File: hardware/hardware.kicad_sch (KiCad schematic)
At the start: 72 parts, among them J1 VBAT+, J10 Conn_01x05_Pin, J2 GND, J3 PHASE_A, J4 PHASE_B, J5 PHASE_C, J6 VBAT+, J7 GND, Q1 SiR158DP, Q10 SiR158DP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

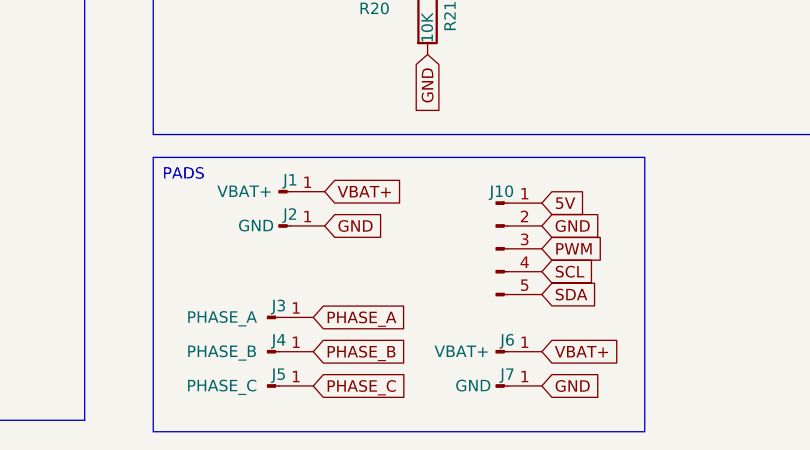
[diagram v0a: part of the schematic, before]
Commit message: add rev1 board - single side
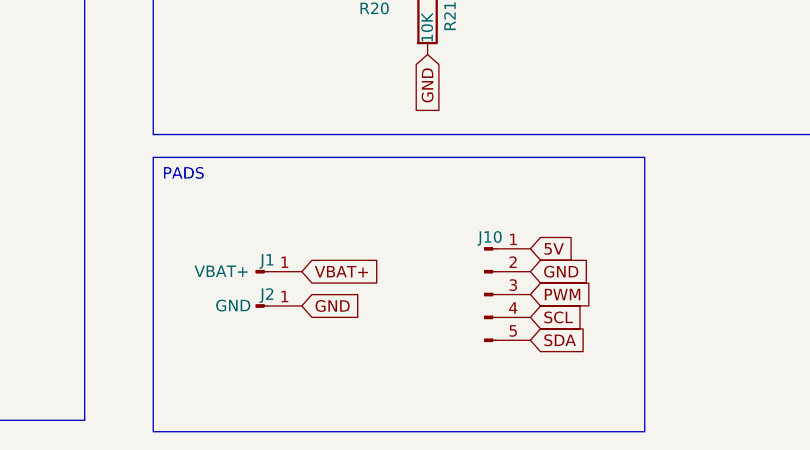
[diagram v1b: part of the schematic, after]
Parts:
- removed J3: PHASE_A, TestPoint:TestPoint_Pad_1.0x1.0mm, symbol Connector:Conn_01x01_Pin
- removed J4: PHASE_B, TestPoint:TestPoint_Pad_1.0x1.0mm, symbol Connector:Conn_01x01_Pin
- removed J5: PHASE_C, TestPoint:TestPoint_Pad_1.0x1.0mm, symbol Connector:Conn_01x01_Pin
- removed J6: VBAT+, TestPoint:TestPoint_Pad_2.0x2.0mm, symbol Connector:Conn_01x01_Pin
- removed J7: GND, TestPoint:TestPoint_Pad_2.0x2.0mm, symbol Connector:Conn_01x01_Pin
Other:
- moved on the sheet: J1, J10, J2

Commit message: add rev2
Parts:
- removed C4: 0.1uF, Capacitor_SMD:C_0805_2012Metric_Pad1.18x1.45mm_HandSolder, symbol Device:C
- removed C5: 1uF, Capacitor_SMD:C_0805_2012Metric_Pad1.18x1.45mm_HandSolder, symbol Device:C
- removed C6, C7, C8, C9: 100uF, Capacitor_Tantalum_SMD:CP_EIA-3216-10_Kemet-I, symbol Device:C_Polarized
- removed D1: BLUE, LED_SMD:LED_0805_2012Metric_Pad1.15x1.40mm_HandSolder, symbol Device:LED
- removed D2: RED, LED_SMD:LED_0805_2012Metric_Pad1.15x1.40mm_HandSolder, symbol Device:LED
- removed J10: Conn_01x05_Pin, Connector_JST:JST_SH_BM05B-SRSS-TB_1x05-1MP_P1.00mm_Vertical, symbol Connector:Conn_01x05_Pin
- removed R10, R8: 3.3K, Resistor_SMD:R_0805_2012Metric_Pad1.20x1.40mm_HandSolder, symbol Device:R
- removed R2, R3: 10K, Resistor_SMD:R_0805_2012Metric_Pad1.20x1.40mm_HandSolder, symbol Device:R
- removed R5: 1K, Resistor_SMD:R_0805_2012Metric_Pad1.20x1.40mm_HandSolder, symbol Device:R
- removed R6: 4.7K, Resistor_SMD:R_0805_2012Metric_Pad1.20x1.40mm_HandSolder, symbol Device:R
- removed R7: 47K, Resistor_SMD:R_0805_2012Metric_Pad1.20x1.40mm_HandSolder, symbol Device:R
- removed R9: 18K, Resistor_SMD:R_0805_2012Metric_Pad1.20x1.40mm_HandSolder, symbol Device:R
- removed TH1: 10K, Resistor_SMD:R_0805_2012Metric_Pad1.20x1.40mm_HandSolder, symbol Device:Thermistor_NTC
- removed U2: ACS7122, Package_SO:SOIC-8_3.9x4.9mm_P1.27mm, symbol Sensor_Current:ACS712xLCTR-30A
- added J3: GND, TestPoint:TestPoint_Keystone_5015_Micro-Minature, symbol Connector:Conn_01x01_Pin
- added J4: PWM, TestPoint:TestPoint_Keystone_5015_Micro-Minature, symbol Connector:Conn_01x01_Pin
- J1: value VBAT+ -> VBAT
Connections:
- net VBAT+ is gone; now on net VBAT: J1.1 (Pin_1), U3.1 (IN)
- net GND: now also J3.1 (Pin_1)
- net PWM: now also J4.1 (Pin_1)
- net CURRENT_ADC: no longer names the net of U1.26 (PC3)
- net LED_STATUS: no longer names the net of U1.14 (PB2)
- net LED_WARN: no longer names the net of U1.13 (PB1)
- net SCL: no longer names the net of U1.28 (PC5)
- net SDA: no longer names the net of U1.27 (PC4)
- net TEMP_ADC: no longer names the net of U1.22 (ADC7)
- net VBAT_ADC: no longer names the net of U1.19 (ADC6)
- no-connect marks 7 -> 13
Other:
- moved on the sheet: C10, C2, C3, J1, J2, R11, R12, R13, R14, R15, R16, R17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

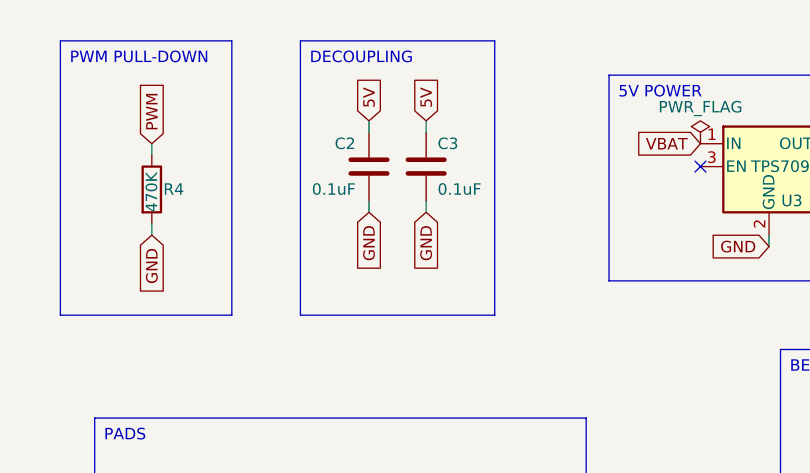
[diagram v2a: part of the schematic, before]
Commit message: rename capacitors
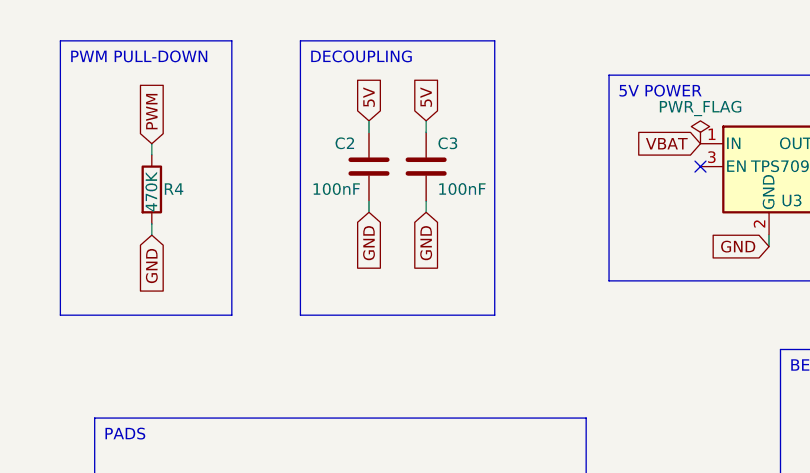
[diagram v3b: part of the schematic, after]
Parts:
- C2, C3: value 0.1uF -> 100nF
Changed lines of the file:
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@@
 			)
 		)
-		(property "Value" "0.1uF"
+		(property "Value" "100nF"
 			(at 156.21 33.02 0)
 			(effects
@@
 			)
 		)
-		(property "Value" "0.1uF"
+		(property "Value" "100nF"
 			(at 170.18 33.02 0)
 			(effects

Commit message: update rev3 board
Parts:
- J3, J4: footprint TestPoint:TestPoint_Keystone_5015_Micro-Minature -> TestPoint:TestPoint_Keystone_5015_Micro_Mini
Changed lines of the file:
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@@
 (kicad_sch
-	(version 20231120)
+	(version 20250114)
 	(generator "eeschema")
-	(generator_version "8.0")
+	(generator_version "9.0")
 	(paper "A4")
 	(title_block
 		(title "NoahESC")
-		(rev "2")
+		(rev "3")
+	)
+	(text_box "MCU"
+		(exclude_from_sim no)
+		(at 15.24 13.97 0)
+		(size 104.14 82.55)
+		(margins 0.9525 0.9525 0.9525 0.9525)
+		(stroke
+			(width 0)
+			(type default)
+		)
+		(fill
+			(type none)
+		)
+		(effects
+			(font
+				(size 1.27 1.27)
+			)
+			(justify left top)
+		)
+	)
+	(text_box "BEMF"
+		(exclude_from_sim no)
+		(at 208.28 50.8 0)
+		(size 58.42 45.72)
+		(margins 0.9525 0.9525 0.9525 0.9525)
+		(stroke
+			(width 0)
+			(type default)
+		)
+		(fill
+			(type none)
+		)
+		(effects
+			(font
+				(size 1.27 1.27)
+			)
+			(justify left top)
+		)
+	)
+	(text_box "5V POWER\n"
+		(exclude_from_sim no)
+		(at 189.23 20.32 0)
+		(size 34.29 22.86)
+		(margins 0.9525 0.9525 0.9525 0.9525)
+		(stroke
+			(width 0)
+			(type default)
+		)
+		(fill
+			(type none)
+		)
+		(effects
+			(font
+				(size 1.27 1.27)
+			)
+			(justify left top)
+		)
+	)
+	(text_box "PADS"
+		(exclude_from_sim no)
+		(at 132.08 58.42 0)
+		(size 54.61 30.48)
+		(margins 0.9525 0.9525 0.9525 0.9525)
+		(stroke
+			(width 0)
+			(type default)
+		)
+		(fill
+			(type none)
+		)
+		(effects
+			(font
+				(size 1.27 1.27)
+			)
+			(justify left top)
+		)
+	)
+	(text_box "DECOUPLING"
+		(exclude_from_sim no)
+		(at 154.94 16.51 0)
+		(size 21.59 30.48)
+		(margins 0.9525 0.9525 0.9525 0.9525)
+		(stroke
+			(width 0)
+			(type default)
+		)
+		(fill
+			(type none)
+		)
+		(effects
+			(font
+				(size 1.27 1.27)
+			)
+			(justify left top)
+		)
+	)
+	(text_box "MOSFET DRIVERS"
+		(exclude_from_sim no)
+		(at 105.41 104.14 0)
+		(size 170.18 55.88)
+		(margins 0.9525 0.9525 0.9525 0.9525)
+		(stroke
+			(width 0)
+			(type default)
+		)
+		(fill
+			(type none)
+		)
+		(effects
+			(font
+				(size 1.27 1.27)
+			)
+			(justify left top)
+		)
+	)
+	(text_box "PWM PULL-DOWN"
+		(exclude_from_sim no)
+		(at 128.27 16.51 0)
+		(size 19.05 30.48)
+		(margins 0.9525 0.9525 0.9525 0.9525)
+		(stroke
+			(width 0)
+			(type default)
+		)
+		(fill
+			(type none)
+		)
+		(effects
+			(font
+				(size 1.27 1.27)
+			)
+			(justify left top)
+		)
+	)
+	(text_box "MOSFETS"
+		(exclude_from_sim no)
+		(at 16.51 100.33 0)
+		(size 81.28 91.44)
+		(margins 0.9525 0.9525 0.9525 0.9525)
+		(stroke
+			(width 0)
+			(type default)
+		)
+		(fill
+			(type none)
+		)
+		(effects
+			(font
+				(size 1.27 1.27)
+			)
+			(justify left top)
+		)
 	)
 	(junction
@@
 		)
 	)
-	(text_box "MCU"
-		(exclude_from_sim no)
-		(at 15.24 13.97 0)
-		(size 104.14 82.55)
-		(stroke
-			(width 0)
-			(type default)
-		)
-		(fill
-			(type none)
-		)
-		(effects
-			(font
-				(size 1.27 1.27)
-			)
-			(justify left top)
-		)
-	)
-	(text_box "BEMF"
-		(exclude_from_sim no)
-		(at 208.28 50.8 0)
-		(size 58.42 45.72)
-		(stroke
-			(width 0)
-			(type default)
-		)
-		(fill
-			(type none)
-		)
-		(effects
-			(font
-				(size 1.27 1.27)
-			)
-			(justify left top)
-		)
-	)
-	(text_box "5V POWER\n"
-		(exclude_from_sim no)
-		(at 189.23 20.32 0)
-		(size 34.29 22.86)
-		(stroke
-			(width 0)
-			(type default)
-		)
-		(fill
-			(type none)
-		)
-		(effects
-			(font
-				(size 1.27 1.27)
-			)
-			(justify left top)
-		)
-	)
-	(text_box "PADS"
-		(exclude_from_sim no)
-		(at 132.08 58.42 0)
-		(size 54.61 30.48)
-		(stroke
-			(width 0)
-			(type default)
-		)
-		(fill
-			(type none)
-		)
-		(effects
-			(font
-				(size 1.27 1.27)
-			)
-			(justify left top)
-		)
-	)
-	(text_box "DECOUPLING"
-		(exclude_from_sim no)
-		(at 154.94 16.51 0)
-		(size 21.59 30.48)
-		(stroke
-			(width 0)
-			(type default)
-		)
-		(fill
-			(type none)
-		)
-		(effects
-			(font
-				(size 1.27 1.27)
-			)
-			(justify left top)
-		)
-	)
-	(text_box "MOSFET DRIVERS"
-		(exclude_from_sim no)
-		(at 105.41 104.14 0)
-		(size 170.18 55.88)
-		(stroke
-			(width 0)
-			(type default)
-		)
-		(fill
-			(type none)
-		)
-		(effects
-			(font
-				(size 1.27 1.27)
-			)
-			(justify left top)
-		)
-	)
-	(text_box "PWM PULL-DOWN"
-		(exclude_from_sim no)
-		(at 128.27 16.51 0)
-		(size 19.05 30.48)
-		(stroke
-			(width 0)
-			(type default)
-		)
-		(fill
-			(type none)
-		)
-		(effects
-			(font
-				(size 1.27 1.27)
-			)
-			(justify left top)
-		)
-	)
-	(text_box "MOSFETS"
-		(exclude_from_sim no)
-		(at 16.51 100.33 0)
-		(size 81.28 91.44)
-		(stroke
-			(width 0)
-			(type default)
-		)
-		(fill
-			(type none)
-		)
-		(effects
-			(font
-				(size 1.27 1.27)
-			)
-			(justify left top)
-		)
-	)
 	(global_label "PWM_BH"
 		(shape input)
@@
 			)
 		)
-		(property "Description" ""
+		(property "Description" "Generic connector, single row, 01x01, script generated"
 			(at 142.24 73.66 0)
 			(effects
@@
 		(fields_autoplaced yes)
 		(property "Reference" "Q9"
-			(at 248.92 124.46 0)
+			(at 248.92 124.4599 0)
 			(effects
 				(font
@@
 		)
 		(property "Value" "BC817"
-			(at 248.92 127 0)
+			(at 248.92 126.9999 0)
 			(effects
 				(font
@@
 			)
 		)
-		(property "Description" ""
+		(property "Description" "0.8A Ic, 45V Vce, NPN Transistor, SOT-23"
 			(at 243.84 125.73 0)
 			(effects
@@
 		(fields_autoplaced yes)
 		(property "Reference" "Q8"
-			(at 193.04 124.46 0)
+			(at 193.04 124.4599 0)
 			(effects
 				(font
@@
 		)
 		(property "Value" "BC817"
-			(at 193.04 127 0)
+			(at 193.04 126.9999 0)
 			(effects
 				(font
@@
 			)
 		)
-		(property "Description" ""
+		(property "Description" "0.8A Ic, 45V Vce, NPN Transistor, SOT-23"
 			(at 187.96 125.73 0)
 			(effects
@@
 			)
 		)
-		(property "Description" ""
+		(property "Description" "Generic connector, single row, 01x01, script generated"
 			(at 142.24 69.85 0)
 			(effects
@@
 		(fields_autoplaced yes)
 		(property "Reference" "Q7"
-			(at 135.89 125.73 0)
+			(at 135.89 125.7299 0)
 			(effects
 				(font
@@
 		)
 		(property "Value" "BC817"
-			(at 135.89 128.27 0)
+			(at 135.89 128.2699 0)
 			(effects
 				(font
@@
 			)
 		)
-		(property "Description" ""
+		(property "Description" "0.8A Ic, 45V Vce, NPN Transistor, SOT-23"
 			(at 130.81 127 0)
 			(effects
@@
 			)
 		)
-		(property "Footprint" "TestPoint:TestPoint_Keystone_5015_Micro-Minature"
+		(property "Footprint" "TestPoint:TestPoint_Keystone_5015_Micro_Mini"
 			(at 163.83 73.66 0)
 			(effects
@@
 			)
 		)
-		(property "Description" ""
+		(property "Description" "Generic connector, single row, 01x01, script generated"
 			(at 163.83 73.66 0)
 			(effects
@@
 			)
 		)
-		(property "Footprint" "TestPoint:TestPoint_Keystone_5015_Micro-Minature"
+		(property "Footprint" "TestPoint:TestPoint_Keystone_5015_Micro_Mini"
 			(at 163.83 68.58 0)
 			(effects
@@
 			)
 		)
-		(property "Description" ""
+		(property "Description" "Generic connector, single row, 01x01, script generated"
 			(at 163.83 68.58 0)
 			(effects
@@
 		)
 	)
+	(embedded_fonts no)
 )

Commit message: add rev4
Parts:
- added J5: Programming, Connector_PinHeader_1.27mm:PinHeader_1x06_P1.27mm_Vertical, symbol Connector:Conn_01x06_Pin
- C10, C11, C12, C13: LCSC (none) -> C28323
- C2, C3: LCSC (none) -> C49678
- D3, D4, D5: LCSC (none) -> C241939
- Q1, Q10, Q2, Q3, Q4, Q5: LCSC (none) -> C142530
- Q7, Q8, Q9: LCSC (none) -> C39828
- R11, R12, R13, R14, R15, R16: LCSC (none) -> C17713
- R17, R18, R19, R22, R25, R30: LCSC (none) -> C17673
- R20, R23, R26, R29, R31, R34: LCSC (none) -> C17408
- R21, R27, R32: LCSC (none) -> C84376
- R24, R28, R33: LCSC (none) -> C17520
- R4: LCSC (none) -> C89104
- U1: LCSC (none) -> C16190
- U3: LCSC (none) -> C2865456
- Y1: LCSC (none) -> C882606
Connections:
- net 5V: now also J5.2 (Pin_2)
- net GND: now also J5.1 (Pin_1)
- net MISO: now reaches U1.16 (PB4)
- net MISO: now also J5.4 (Pin_4)
- net SCK: now reaches U1.17 (PB5)
- net SCK: now also J5.6 (Pin_6)
- net RESET: now reaches U1.29 (PC6/~{RESET})
- net RESET: now also J5.3 (Pin_3)
- net PWM_CL renamed MOSI
- net MOSI: now also J5.5 (Pin_5)
- no-connect marks 13 -> 10
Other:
- moved on the sheet: J1, J2, J3, J4

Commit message: add new pwm pin
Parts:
- removed J3: GND, TestPoint:TestPoint_Keystone_5015_Micro_Mini, symbol Connector:Conn_01x01_Pin
- removed J4: PWM, TestPoint:TestPoint_Keystone_5015_Micro_Mini, symbol Connector:Conn_01x01_Pin
- added J6: PWM, Connector_PinHeader_2.54mm:PinHeader_1x02_P2.54mm_Vertical, symbol Connector:Conn_01x02_Pin
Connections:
- net GND: now also J6.1 (Pin_1)
- net PWM: now also J6.2 (Pin_2)
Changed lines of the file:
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@@
 		)
 	)
-	(global_label "PWM"
-		(shape input)
-		(at 147.32 81.28 0)
-		(fields_autoplaced yes)
-		(effects
-			(font
-				(size 1.27 1.27)
-			)
-			(justify left)
-		)
-		(property "Intersheetrefs" "${INTERSHEET_REFS}"
-			(at 154.478 81.28 0)
-			(effects
-				(font
-					(size 1.27 1.27)
-				)
-				(justify left)
-				(hide yes)
-			)
-		)
-	)
 	(global_label "PWM_BL"
 		(shape input)
@@
 		)
 	)
+	(global_label "PWM"
+		(shape input)
+		(at 144.78 80.01 0)
+		(fields_autoplaced yes)
+		(effects
+			(font
+				(size 1.27 1.27)
+			)
+			(justify left)
+		)
+		(property "Intersheetrefs" "${INTERSHEET_REFS}"
+			(at 151.938 80.01 0)
+			(effects
+				(font
+					(size 1.27 1.27)
+				)
+				(justify left)
+				(hide yes)
+			)
+		)
+	)
 	(global_label "PWM_BL"
 		(shape input)
@@
 	(global_label "GND"
 		(shape input)
+		(at 144.78 77.47 0)
+		(fields_autoplaced yes)
+		(effects
+			(font
+				(size 1.27 1.27)
+			)
+			(justify left)
+		)
+		(property "Intersheetrefs" "${INTERSHEET_REFS}"
+			(at 151.6357 77.47 0)
+			(effects
+				(font
+					(size 1.27 1.27)
+				)
+				(justify left)
+				(hide yes)
+			)
+		)
+	)
+	(global_label "GND"
+		(shape input)
 		(at 39.37 132.08 270)
 		(fields_autoplaced yes)
@@
 		)
 	)
-	(global_label "GND"
-		(shape input)
-		(at 147.32 76.2 0)
-		(fields_autoplaced yes)
-		(effects
-			(font
-				(size 1.27 1.27)
-			)
-			(justify left)
-		)
-		(property "Intersheetrefs" "${INTERSHEET_REFS}"
-			(at 154.1757 76.2 0)
-			(effects
-				(font
-					(size 1.27 1.27)
-				)
-				(justify left)
-				(hide yes)
-			)
-		)
-	)
 	(global_label "GATE_AH"
 		(shape input)
@@
 	)
 	(symbol
+		(lib_id "Connector:Conn_01x02_Pin")
+		(at 139.7 77.47 0)
+		(unit 1)
+		(exclude_from_sim no)
+		(in_bom yes)
+		(on_board yes)
+		(dnp no)
+		(property "Reference" "J6"
+			(at 141.224 74.93 0)
+			(effects
+				(font
+					(size 1.27 1.27)
+				)
+			)
+		)
+		(property "Value" "PWM"
+			(at 136.144 78.74 0)
+			(effects
+				(font
+					(size 1.27 1.27)
+				)
+			)
+		)
+		(property "Footprint" "Connector_PinHeader_2.54mm:PinHeader_1x02_P2.54mm_Vertical"
+			(at 139.7 77.47 0)
+			(effects
+				(font
+					(size 1.27 1.27)
+				)
+				(hide yes)
+			)
+		)
+		(property "Datasheet" "~"
+			(at 139.7 77.47 0)
+			(effects
+				(font
+					(size 1.27 1.27)
+				)
+				(hide yes)
+			)
+		)
+		(property "Description" "Generic connector, single row, 01x02, script generated"
+			(at 139.7 77.47 0)
+			(effects
+				(font
+					(size 1.27 1.27)
+				)
+				(hide yes)
+			)
+		)
+		(property "LCSC" "C42431798"
+			(at 139.7 77.47 0)
+			(effects
+				(font
+					(size 1.27 1.27)
+				)
+				(hide yes)
+			)
+		)
+		(pin "1"
+		)
+		(pin "2"
+		)
+		(instances
+			(project ""
+				(path "/db766d7c-2ba8-4022-adcf-07c3b0e5779a"
+					(reference "J6")
+					(unit 1)
+				)
+			)
+		)
+	)
+	(symbol
 		(lib_id "Device:C")
 		(at 162.56 30.48 0)
@@
 	)
 	(symbol
-		(lib_id "Connector:Conn_01x01_Pin")
-		(at 142.24 81.28 0)
-		(unit 1)
-		(exclude_from_sim no)
-		(in_bom yes)
-		(on_board yes)
-		(dnp no)
-		(property "Reference" "J4"
-			(at 143.002 79.756 0)
-			(effects
-				(font
-					(size 1.27 1.27)
-				)
-			)
-		)
-		(property "Value" "PWM"
-			(at 139.7 81.28 0)
-			(effects
-				(font
-					(size 1.27 1.27)
-				)
-			)
-		)
-		(property "Footprint" "TestPoint:TestPoint_Keystone_5015_Micro_Mini"
-			(at 142.24 81.28 0)
-			(effects
-				(font
-					(size 1.27 1.27)
-				)
-				(hide yes)
-			)
-		)
-		(property "Datasheet" "~"
-			(at 142.24 81.28 0)
-			(effects
-				(font
-					(size 1.27 1.27)
-				)
-				(hide yes)
-			)
-		)
-		(property "Description" "Generic connector, single row, 01x01, script generated"
-			(at 142.24 81.28 0)
-			(effects
-				(font
-					(size 1.27 1.27)
-				)
-				(hide yes)
-			)
-		)
-		(pin "1"
-		)
-		(instances
-			(project "hardware"
-				(path "/db766d7c-2ba8-4022-adcf-07c3b0e5779a"
-					(reference "J4")
-					(unit 1)
-				)
-			)
-		)
-	)
-	(symbol
 		(lib_id "Device:C")
 		(at 214.63 31.75 180)
@@
 					(unit 1)
 				)
-			)
-		)
-	)
-	(symbol
-		(lib_id "Connector:Conn_01x01_Pin")
-		(at 142.24 76.2 0)
-		(unit 1)
-		(exclude_from_sim no)
-		(in_bom yes)
-		(on_board yes)
-		(dnp no)
-		(property "Reference" "J3"
-			(at 143.002 74.676 0)
-			(effects
-				(font
-					(size 1.27 1.27)
-				)
-			)
-		)
-		(property "Value" "GND"
-			(at 139.7 76.2 0)
-			(effects
-				(font
-					(size 1.27 1.27)
-				)
-			)
-		)
-		(property "Footprint" "TestPoint:TestPoint_Keystone_5015_Micro_Mini"
-			(at 142.24 76.2 0)
-			(effects
-				(font
-					(size 1.27 1.27)
-				)
-				(hide yes)
-			)
-		)
-		(property "Datasheet" "~"
-			(at 142.24 76.2 0)
-			(effects
-				(font
-					(size 1.27 1.27)
-				)
-				(hide yes)
-			)
-		)
-		(property "Description" "Generic connector, single row, 01x01, script generated"
-			(at 142.24 76.2 0)
-			(effects
-				(font
-					(size 1.27 1.27)
-				)
-				(hide yes)
-			)
-		)
-		(pin "1"
-		)
-		(instances
-			(project "hardware"
-				(path "/db766d7c-2ba8-4022-adcf-07c3b0e5779a"
-					(reference "J3")
-					(unit 1)
-				)
